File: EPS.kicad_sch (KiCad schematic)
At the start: 4 parts, among them J101 Conn_01x04, J102 Conn_01x20

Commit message: progress on switch sheet
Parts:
- removed J102: Conn_01x20, symbol Connector_Generic:Conn_01x20
- added J101, J102: Conn_02x26_Odd_Even, symbol Connector_Generic:Conn_02x26_Odd_Even
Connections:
- net GND: now also J102.29 (Pin_29), J102.30 (Pin_30), J102.32 (Pin_32)
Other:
- removed sheet Power_Conditioning
- sheet Channel_Matrix ports: added AMEAS_Chan_O_1, AMEAS_Chan_O_2, Channel_O_EN_1, Channel_O_EN_2; removed Channel_O_3V3_EN_1, Channel_O_3V3_EN_2, Channel_O_5V_EN_1, Channel_O_5V_EN_2

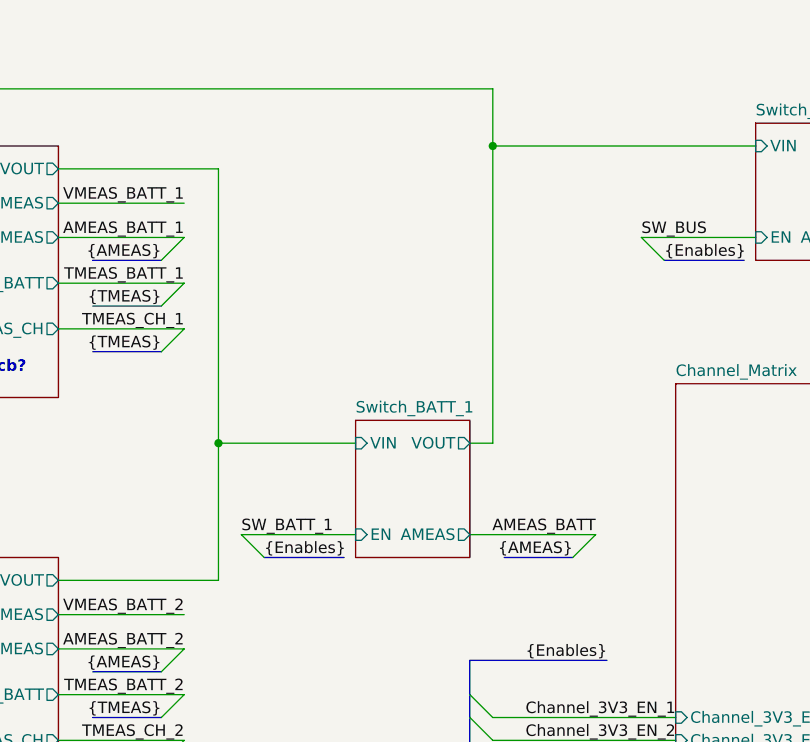
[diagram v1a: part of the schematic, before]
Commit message: added possible parts to switch sheet
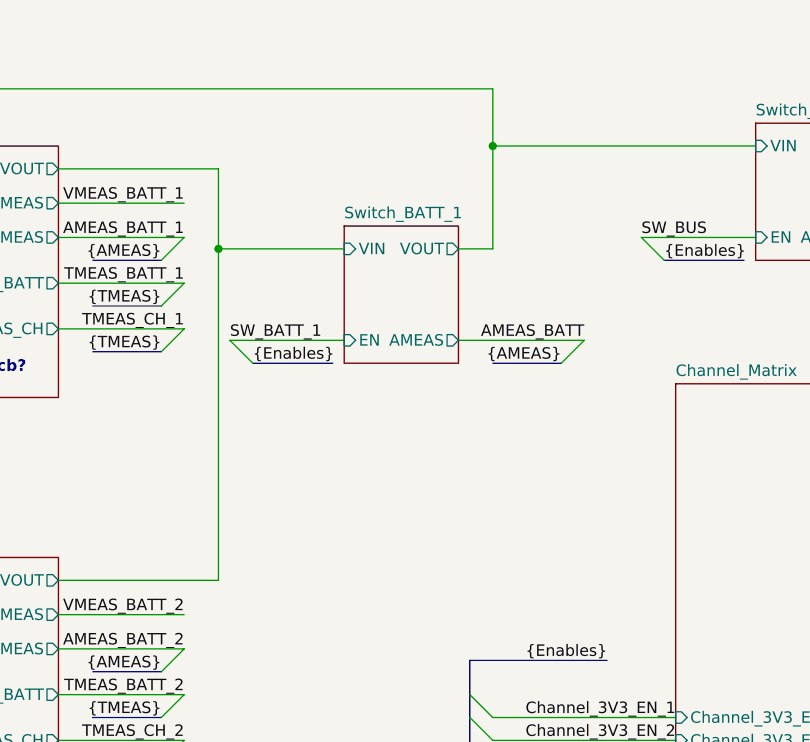
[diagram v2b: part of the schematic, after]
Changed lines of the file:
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@@
 	)
 	(junction
+		(at 175.26 36.83)
+		(diameter 0)
+		(color 0 0 0 0)
+	)
+	(junction
 		(at 149.86 157.48)
 		(diameter 0)
@@
 	)
 	(junction
-		(at 175.26 58.42)
-		(diameter 0)
-		(color 0 0 0 0)
-	)
-	(junction
 		(at 91.44 59.69)
 		(diameter 0)
@@
 	)
 	(bus_entry
-		(at 177.8 68.58)
+		(at 176.53 46.99)
 		(size 2.54 2.54)
 		(stroke
@@
 	)
 	(bus_entry
-		(at 214.63 71.12)
+		(at 213.36 49.53)
 		(size 2.54 -2.54)
 		(stroke
@@
 	(wire
 		(pts
-			(xy 175.26 58.42) (xy 175.26 27.94)
-		)
-		(stroke
-			(width 0)
-			(type default)
-		)
-	)
-	(wire
-		(pts
 			(xy 111.76 31.75) (xy 129.54 31.75)
 		)
@@
 		)
 	)
+	(wire
+		(pts
+			(xy 175.26 36.83) (xy 175.26 27.94)
+		)
+		(stroke
+			(width 0)
+			(type default)
+		)
+	)
 	(bus
 		(pts
@@
 	(wire
 		(pts
+			(xy 175.26 36.83) (xy 175.26 73.66)
+		)
+		(stroke
+			(width 0)
+			(type default)
+		)
+	)
+	(wire
+		(pts
 			(xy 205.74 113.03) (xy 226.06 113.03)
 		)
@@
 	(wire
 		(pts
-			(xy 205.74 58.42) (xy 205.74 25.4)
+			(xy 205.74 36.83) (xy 205.74 25.4)
 		)
 		(stroke
@@
 	(bus
 		(pts
-			(xy 207.01 71.12) (xy 214.63 71.12)
+			(xy 205.74 49.53) (xy 213.36 49.53)
 		)
 		(stroke
@@
 	(wire
 		(pts
-			(xy 217.17 68.58) (xy 203.2 68.58)
+			(xy 215.9 46.99) (xy 201.93 46.99)
 		)
 		(stroke
@@
 	(wire
 		(pts
-			(xy 205.74 58.42) (xy 203.2 58.42)
+			(xy 205.74 36.83) (xy 201.93 36.83)
 		)
 		(stroke
@@
 	(wire
 		(pts
-			(xy 175.26 58.42) (xy 190.5 58.42)
+			(xy 175.26 36.83) (xy 189.23 36.83)
 		)
 		(stroke
@@
 	(wire
 		(pts
-			(xy 177.8 68.58) (xy 190.5 68.58)
+			(xy 176.53 46.99) (xy 189.23 46.99)
 		)
 		(stroke
@@
 	(bus
 		(pts
-			(xy 180.34 71.12) (xy 189.23 71.12)
+			(xy 179.07 49.53) (xy 187.96 49.53)
 		)
 		(stroke
@@
 	(wire
 		(pts
-			(xy 175.26 58.42) (xy 175.26 73.66)
-		)
-		(stroke
-			(width 0)
-			(type default)
-		)
-	)
-	(wire
-		(pts
 			(xy 111.76 77.47) (xy 129.54 77.47)
 		)
@@
 	)
 	(label "SW_BATT_1"
-		(at 177.8 68.58 0)
+		(at 176.53 46.99 0)
 		(effects
 			(font
@@
 	)
 	(label "{Enables}"
-		(at 180.34 71.12 0)
+		(at 179.07 49.53 0)
 		(effects
 			(font
@@
 	)
 	(label "AMEAS_BATT"
-		(at 217.17 68.58 180)
+		(at 215.9 46.99 180)
 		(effects
 			(font
@@
 	)
 	(label "{AMEAS}"
-		(at 214.63 71.12 180)
+		(at 213.36 49.53 180)
 		(effects
 			(font
@@
 	)
 	(sheet
-		(at 190.5 55.88)
+		(at 189.23 34.29)
 		(size 12.7 15.24)
 		(exclude_from_sim no)
@@
 		)
 		(property "Sheetname" "Switch_BATT_1"
-			(at 190.5 55.1684 0)
+			(at 189.23 33.5784 0)
 			(effects
 				(font
@@
 		)
 		(property "Sheetfile" "Switch.kicad_sch"
-			(at 190.5 71.7046 0)
+			(at 189.23 50.1146 0)
 			(effects
 				(font
@@
 		)
 		(pin "EN" input
-			(at 190.5 68.58 180)
+			(at 189.23 46.99 180)
 			(effects
 				(font
@@
 		)
 		(pin "VIN" input
-			(at 190.5 58.42 180)
+			(at 189.23 36.83 180)
 			(effects
 				(font
@@
 		)
 		(pin "VOUT" output
-			(at 203.2 58.42 0)
+			(at 201.93 36.83 0)
 			(effects
 				(font
@@
 		)
 		(pin "AMEAS" output
-			(at 203.2 68.58 0)
+			(at 201.93 46.99 0)
 			(effects
 				(font

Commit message: specified design
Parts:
- removed BT101: Battery, symbol Device:Battery
- removed H101: PCB Outline, Outlines:SPACEMANIC_V1c, symbol Mechanical:MountingHole
- removed J101: Conn_01x04, symbol Connector_Generic:Conn_01x04
- removed J101, J102: Conn_02x26_Odd_Even, symbol Connector_Generic:Conn_02x26_Odd_Even
- added C101: 1n, Capacitor_SMD:C_0805_2012Metric_Pad1.18x1.45mm_HandSolder, symbol Device:C_Small
- added H101, H102, H103, H104, H105, H106, H107, H108, H109, H110, H111, H112: MountingHole, MountingHole:MountingHole_3.2mm_M3_Pad_Via, symbol Mechanical:MountingHole_Pad
- added PCB101, PCB102, PCB103: PCB Outline, Outlines:SPACEMANIC_V1c, symbol Mechanical:MountingHole
- added R101: 1M, Resistor_SMD:R_0603_1608Metric_Pad0.98x0.95mm_HandSolder, symbol Device:R_Small
- added R102, R104: 100k, Resistor_SMD:R_0603_1608Metric_Pad0.98x0.95mm_HandSolder, symbol Device:R_Small
- added R103, R105: TBD, Resistor_SMD:R_0603_1608Metric_Pad0.98x0.95mm_HandSolder, symbol Device:R_Small
- added SW101: Deploy_1, symbol Switch:SW_Push
- added SW102: Deploy_2, symbol Switch:SW_Push
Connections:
- net GND: now also C101.2, R101.2, SW101.1, SW102.1
- new net: R103.1, SW101.2
- new net: R105.1, SW102.2
- new net BATT: R104.2
- new net BUS: R102.2
- new net SHIELD: C101.1, H101.1, H102.1, H103.1, H104.1, H105.1, H106.1, H107.1, H108.1, H109.1, H110.1, H111.1, H112.1, R101.1
- new net Switch_Deploy_BATT/EN: R104.1, R105.2
- new net Switch_Deploy_BUS/EN: R102.1, R103.2
- no-connect marks 3 -> 5
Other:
- sheet Battery_Cell_Input_2 renamed Battery_Input_2
- sheet CPU renamed MCU
- removed sheet Switch_BUS_1
- removed sheet Switch_SOL_1
- removed sheet Switch_SOL_2
- removed sheet Switch_SOL_3
- added sheet Interface (Interface.kicad_sch)
- added sheet Switch_BATT_2 (Switch_H.kicad_sch)
- added sheet Switch_Deploy_BATT (Switch_H.kicad_sch)
- added sheet Switch_Deploy_BUS (Switch_H.kicad_sch)
- sheet Battery_Input_1 ports: added none; removed AMEAS, Batt, TMEAS_CH, VIN, VOUT
- sheet Battery_Input_2 ports: added none; removed AMEAS, Batt, TMEAS_CH, VIN, VOUT
- sheet Channel_Matrix ports: added {AMEAS}, {Channels}, {Enables}; removed AMEAS_Chan_O_1, AMEAS_Chan_O_2, Channel_1, Channel_2, Channel_3V3_EN_1, Channel_3V3_EN_2, Channel_3v3_1, Channel_3v3_2, Channel_5V_1, Channel_5V_2, Channel_5V_EN_1, Channel_5V_EN_2, Channel_O_EN_1, Channel_O_EN_2
- sheet MCU: file CPU.kicad_sch -> MCU.kicad_sch
- sheet MCU ports: added CS, MISO, MOSI, SCK, {AMEAS}, {Enables}, {TMEAS}, {VMEAS}; removed AMEAS, Enables, TMEAS
- sheet Solar_input_1 ports: added PV_IN, PWM, TOGGLE; removed none
- sheet Solar_input_2 ports: added PV_IN, PWM, TOGGLE; removed none
- sheet Solar_input_3 ports: added PV_IN, PWM, TOGGLE; removed none
- sheet Switch_BATT_1: file Switch.kicad_sch -> Switch_H.kicad_sch
- sheet Switch_BATT_1 ports: added VIN1, VIN2, ~{ALERT}; removed VIN
- note added: "Connector"
- note removed: "Move to external pcb?"

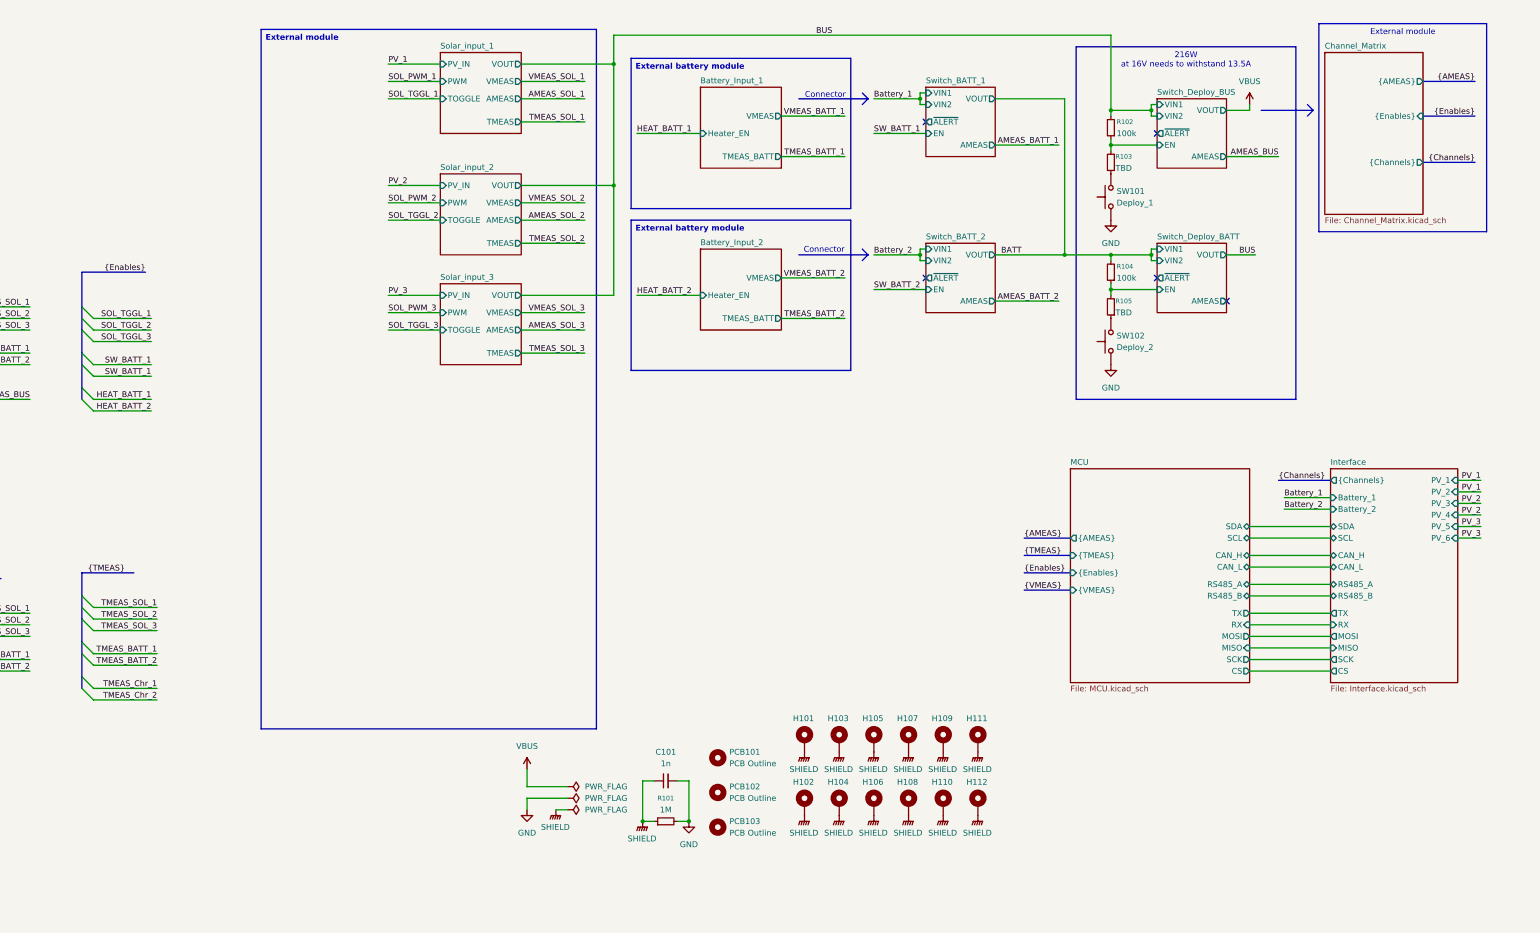
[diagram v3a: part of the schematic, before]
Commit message: added second AMUX and housekeeping
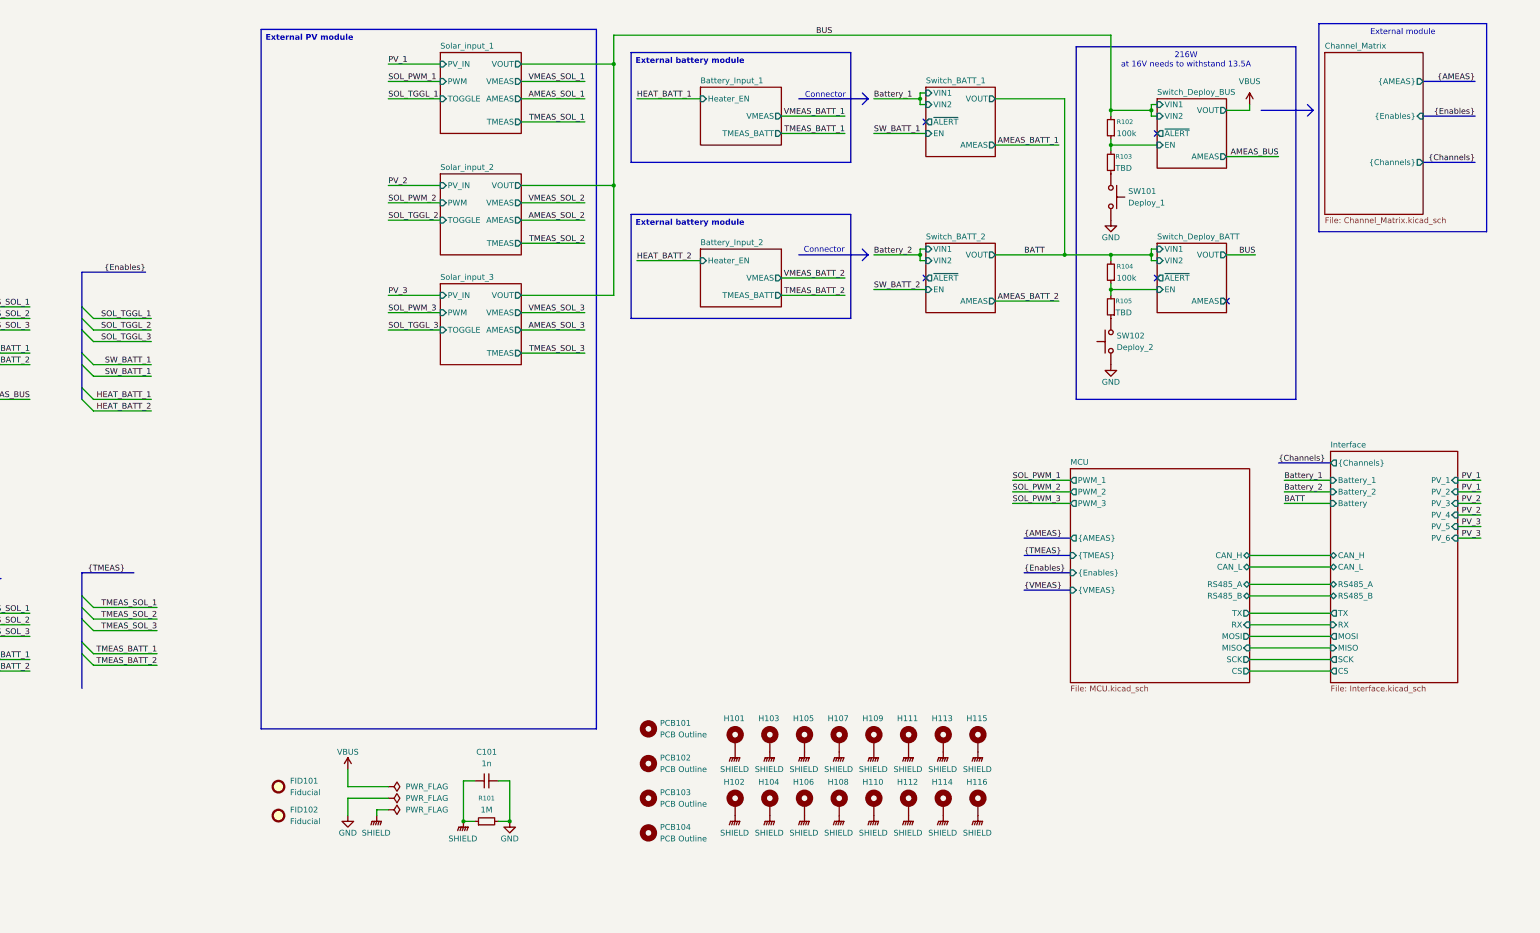
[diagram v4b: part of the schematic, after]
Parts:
- added FID101, FID102: Fiducial, symbol Mechanical:Fiducial
- added H113, H114, H115, H116: MountingHole, MountingHole:MountingHole_3.2mm_M3_Pad_Via, symbol Mechanical:MountingHole_Pad
- added PCB104: PCB Outline, Outlines:SPACEMANIC_V1c, symbol Mechanical:MountingHole
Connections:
- net GND: now also SW101.2; no longer SW101.1
- net SHIELD: now also H113.1, H114.1, H115.1, H116.1
- net at R103.1: now also SW101.1; no longer SW101.2
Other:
- sheet Interface ports: added Battery; removed SCL, SDA
- sheet MCU ports: added PWM_1, PWM_2, PWM_3; removed SCL, SDA
- moved on the sheet: C101, H101, H102, H103, H104, H105, H106, H107, H108, H109, H110, H111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
